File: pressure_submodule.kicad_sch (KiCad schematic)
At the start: 23 parts, among them IC1 PINA350ABSIDDFR, J3 Conn_01x04, Q1 BSZ0902NSATMA1

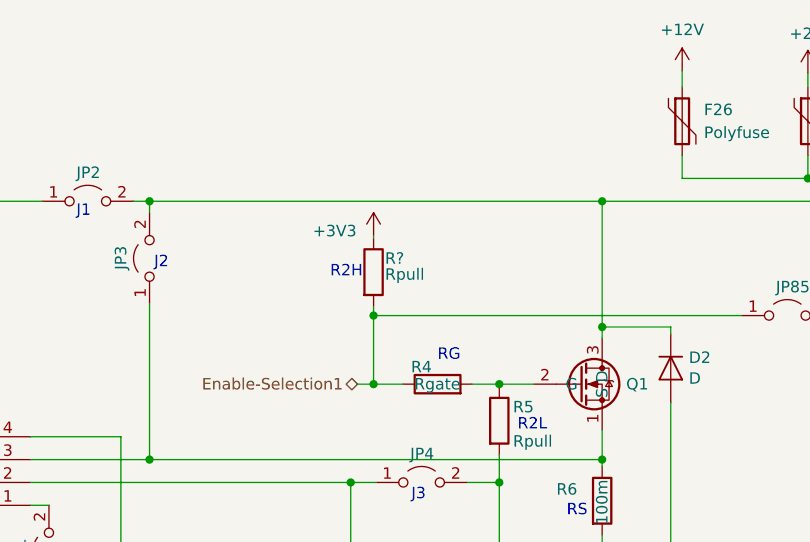
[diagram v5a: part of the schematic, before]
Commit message: IOBv4 JLCPCB ordered on 15.03.2023
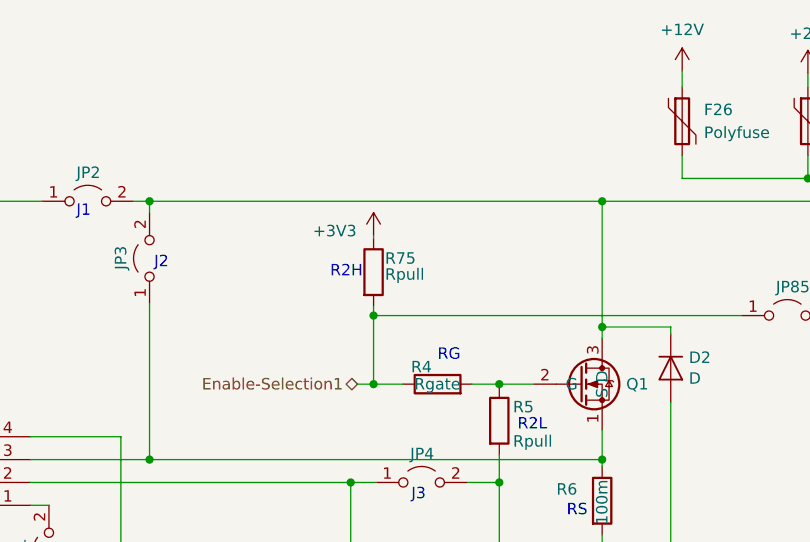
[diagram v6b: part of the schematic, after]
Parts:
- gave numbers to parts that had none: 1
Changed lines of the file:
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@@
   (symbol (lib_id "Device:R") (at 142.494 61.468 0) (unit 1)
     (in_bom yes) (on_board yes)
-    (property "Reference" "R?" (id 0) (at 143.764 59.944 0)
+    (property "Reference" "R75" (id 0) (at 143.764 59.944 0)
       (effects (font (size 1.27 1.27)) (justify left))
     )
@@
   (symbol (lib_id "power:+3V3") (at 142.494 57.404 0) (unit 1)
     (in_bom yes) (on_board yes)
-    (property "Reference" "#PWR?" (id 0) (at 142.494 61.214 0)
-      (effects (font (size 1.27 1.27)) hide)
-    )
+    (property "Reference" "#PWR028" (id 0) (at 142.494 61.214 0)
+      (effects (font (size 1.27 1.27)) hide)
+    )
